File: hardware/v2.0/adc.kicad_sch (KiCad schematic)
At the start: 19 parts, among them IC2 LTC2256CUJ-12#PBF, J7 RSP-122811-01, U1 ECP5U-25F-CABGA256, U11 LT1993CUD-2_PBF, Y2 SG-8018CG 50.000000MHz

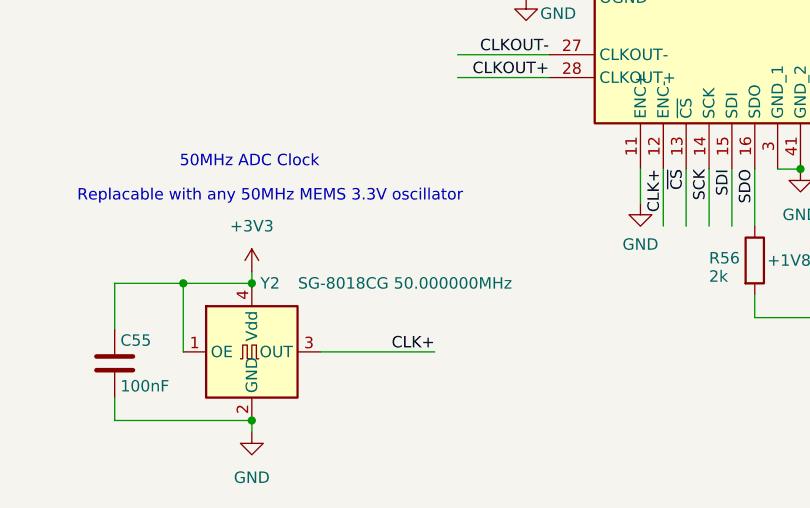
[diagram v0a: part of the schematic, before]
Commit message: HPD line protection
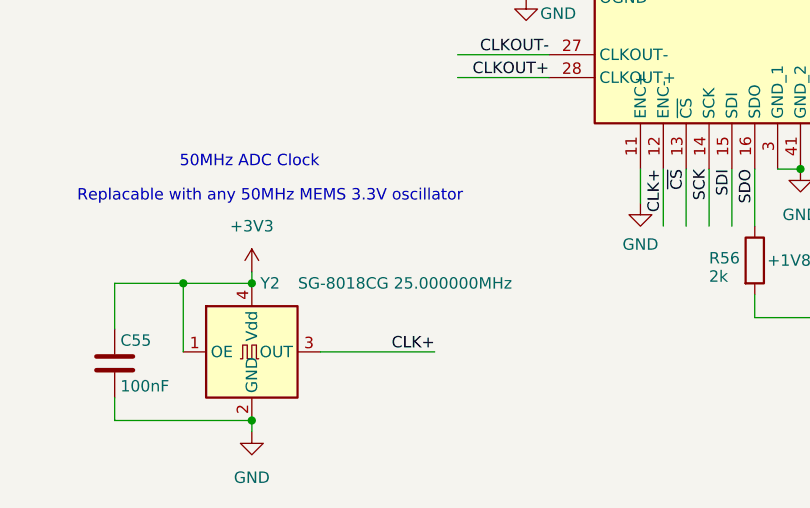
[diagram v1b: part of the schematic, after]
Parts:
- Y2: value SG-8018CG 50.000000MHz -> SG-8018CG 25.000000MHz; LCSC Link https://lcsc.com/product-detail/Programmable-Oscillators_EP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 -> https://www.lcsc.com/product-detail/C21113871.html; LCSC Part # C390526 -> C21113871; Manufactuer Part Number SG-8018CG 50.000000MHz TJHSA -> SG-8018CG 25.0000M-TJHPA3
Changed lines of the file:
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@@
 			)
 		)
-		(property "Value" "SG-8018CG 50.000000MHz"
+		(property "Value" "SG-8018CG 25.000000MHz"
 			(at 110.998 148.59 0)
 			(effects
@@
 			)
 		)
-		(property "LCSC Part #" "C390526"
+		(property "LCSC Part #" "C21113871"
 			(at 93.98 156.21 0)
 			(effects
@@
 			)
 		)
-		(property "LCSC Link" "https://lcsc.com/product-detail/Programmable-Oscillators_EPSON-SG-8018CG-50-000000MHz-TJHSA_C390526.html"
+		(property "LCSC Link" "https://www.lcsc.com/product-detail/C21113871.html"
 			(at 93.98 156.21 0)
 			(effects
@@
 			)
 		)
-		(property "Manufactuer Part Number" "SG-8018CG 50.000000MHz TJHSA"
+		(property "Manufactuer Part Number" "SG-8018CG 25.0000M-TJHPA3"
 			(at 93.98 156.21 0)
 			(effects

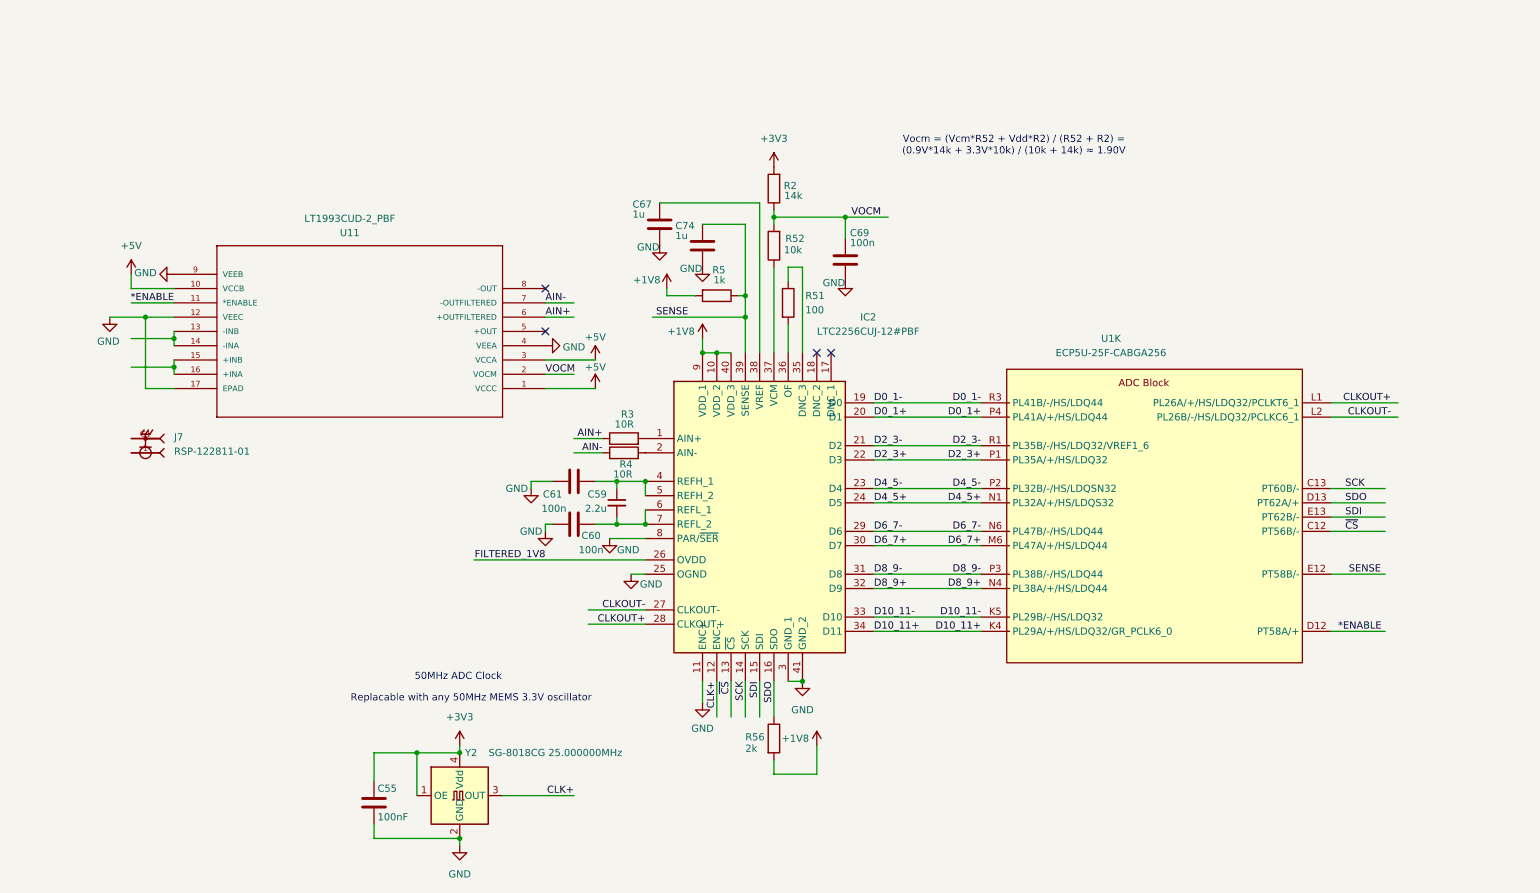
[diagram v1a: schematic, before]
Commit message: ADC driver power and signal input
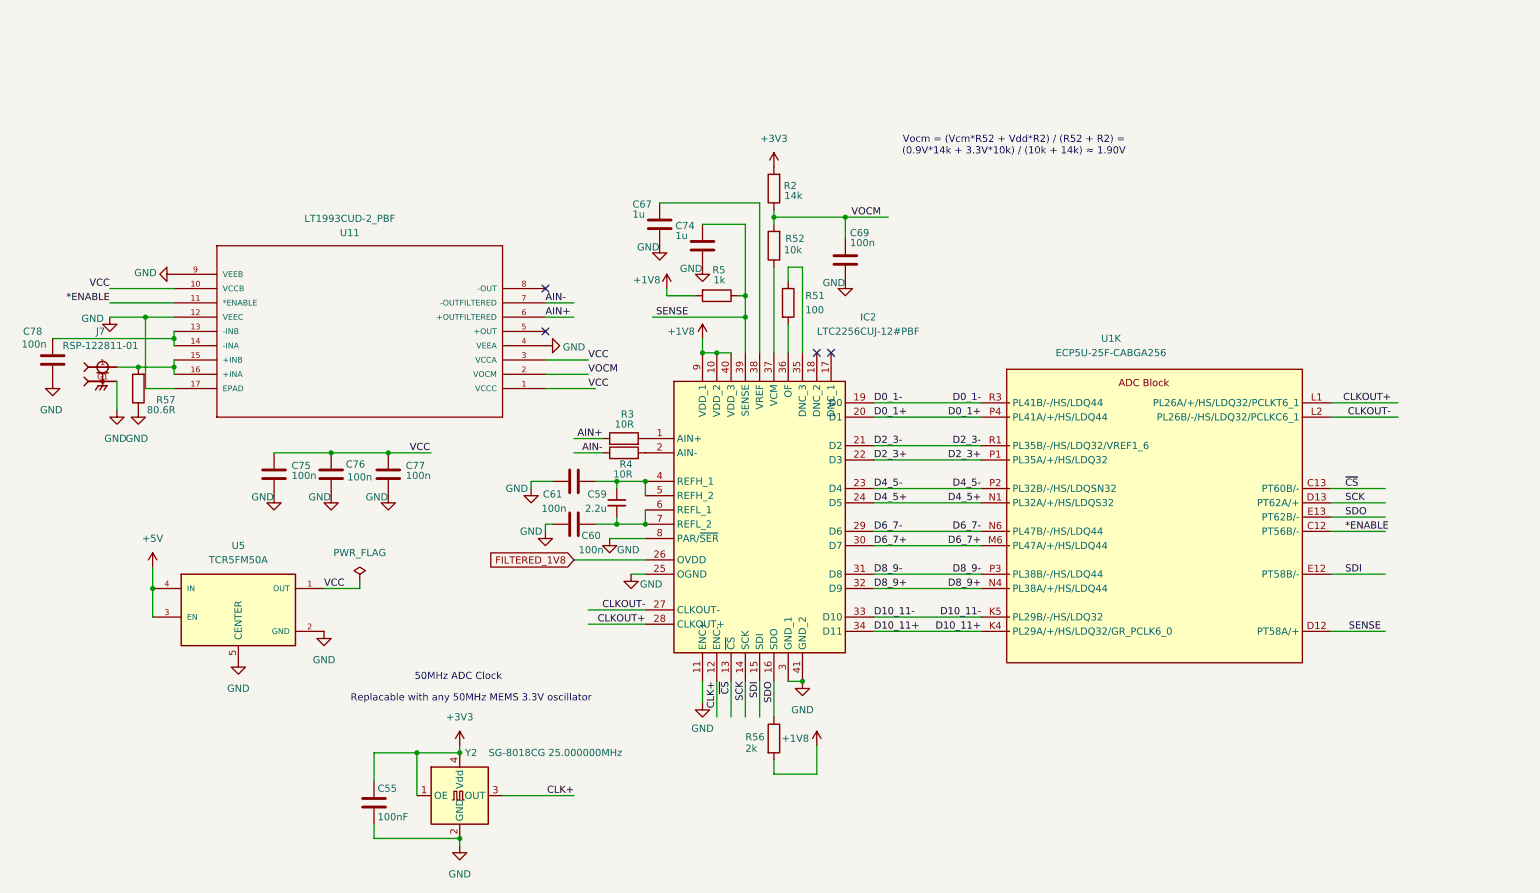
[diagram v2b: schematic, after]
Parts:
- added C75, C76, C77, C78: 100n, Capacitor_SMD:C_0402_1005Metric, symbol Device:C
- added R57: 80.6R, Resistor_SMD:R_0402_1005Metric, symbol Device:R
- added U5: TCR5FM50A, TCR5FM50A:TCR5FM50A, symbol TCR5FM50A:TCR5FM50A
- R3: LCSC Link https://www.lcsc.com/product-detail/C17326083.htm -> https://www.lcsc.com/product-detail/C17693045.html; LCSC Part # C17326083 -> C17693045; Manufactuer Part Number RCS1005F100CS -> RC1005F100CS
- R4: LCSC Link https://www.lcsc.com/product-detail/C17326083.html -> https://www.lcsc.com/product-detail/C17693045.html; LCSC Part # C17326083 -> C17693045; Manufactuer Part Number RCS1005F100CS -> RC1005F100CS
- U11: footprint LT1993CUD-2_PBF:QFN-16_UD -> LT1993CUD_2_PBF:QFN-16_UD
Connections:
- net *ENABLE: now also U1.C12 (PT56B/-); no longer U1.D12 (PT58A/+)
- net +5V: now also U5.3 (EN), U5.4 (IN); no longer U11.1 (VCCC), U11.10 (VCCB), U11.3 (VCCA)
- net GND: now also J7.G1, J7.G2, C75.2, C76.2, C77.2, C78.1, R57.1, U5.2 (GND), U5.5 (CENTER)
- net SCK: now also U1.D13 (PT62A/+); no longer U1.C13 (PT60B/-)
- net SDI: now also U1.E12 (PT58B/-); no longer U1.E13 (PT62B/-)
- net SDO: now also U1.E13 (PT62B/-); no longer U1.D13 (PT62A/+)
- net SENSE: now also U1.D12 (PT58A/+); no longer U1.E12 (PT58B/-)
- net ~{CS}: now also U1.C13 (PT60B/-); no longer U1.C12 (PT56B/-)
- net at U11.13 (-INB), U11.14 (-INA): now also C78.2
- net at U11.15 (+INB), U11.16 (+INA): now also J7.1, R57.2
- new net VCC: C75.1, C76.1, C77.1, U11.1 (VCCC), U11.10 (VCCB), U11.3 (VCCA), U5.1 (OUT)
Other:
- moved on the sheet: J7

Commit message: BOM fields unification for PCBWay requirements
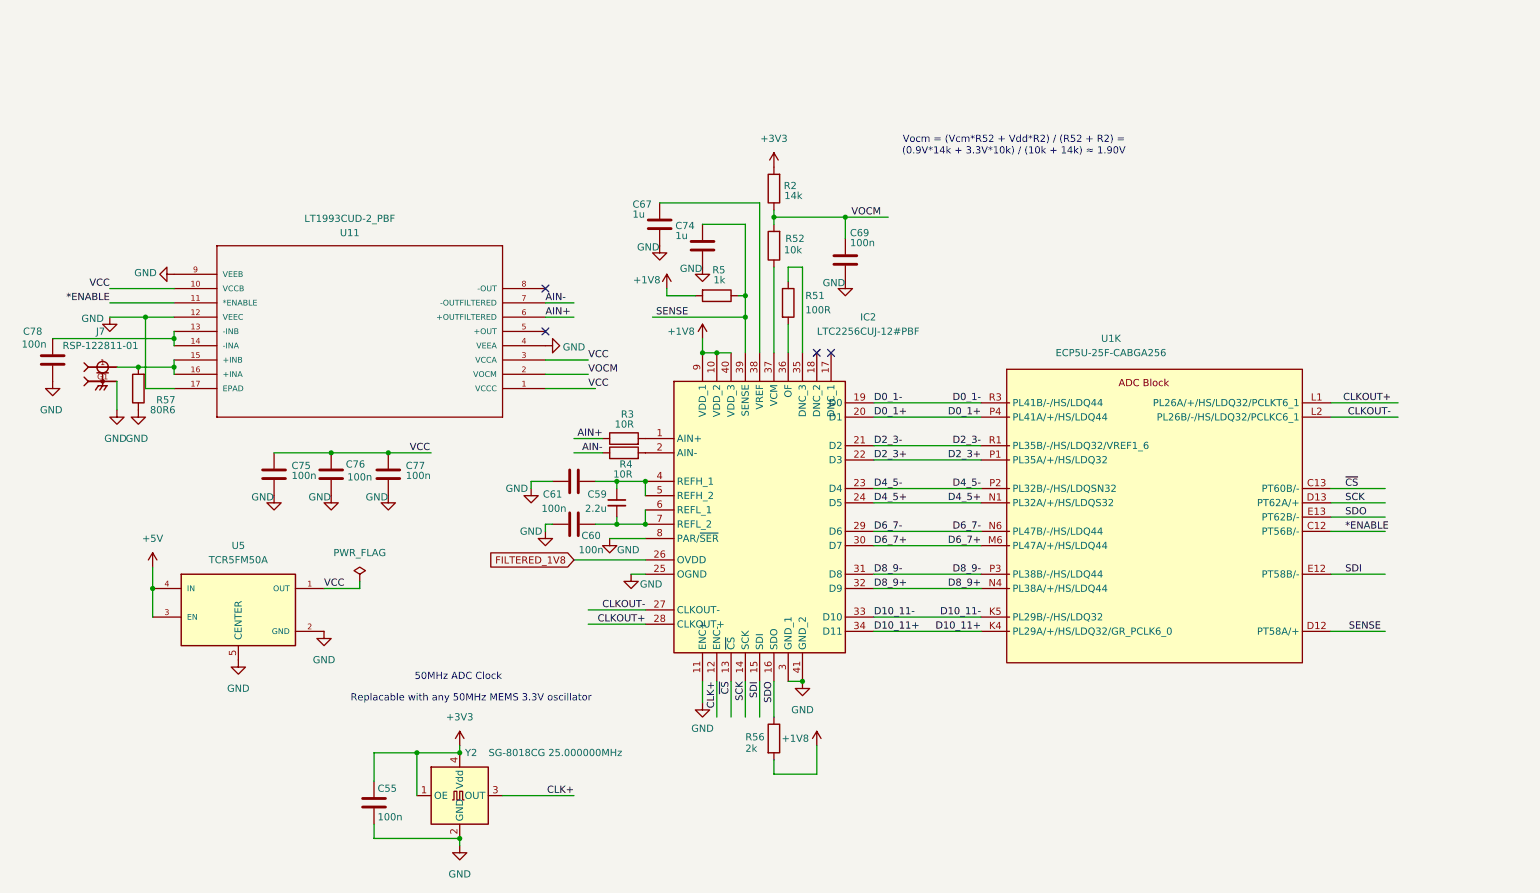
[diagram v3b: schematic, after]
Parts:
- C55: value 100nF -> 100n; MANUFACTURER (none) -> Samsung Electro-Mechanics; MANUFACTURER_PART_NUMBER (none) -> CL05B104KB54PNC
- C59: MANUFACTURER (none) -> Samsung Electro-Mechanics; MANUFACTURER_PART_NUMBER (none) -> CL10A225KP8NNNC
- C60, C61, C69, C75, C76, C77, C78: MANUFACTURER (none) -> Samsung Electro-Mechanics; MANUFACTURER_PART_NUMBER (none) -> CL05B104KB54PNC
- C67, C74: MANUFACTURER (none) -> YAGEO; MANUFACTURER_PART_NUMBER (none) -> CC0402KRX5R6BB105
- IC2: MANUFACTURER (none) -> ADI; MANUFACTURER_PART_NUMBER (none) -> LTC2256CUJ-12#PBF
- J7: MANUFACTURER_PART_NUMBER (none) -> RSP-122811-01
- R2: MANUFACTURER (none) -> UNI-ROYAL; MANUFACTURER_PART_NUMBER (none) -> 0402WGF1402TCE
- R3, R4: MANUFACTURER (none) -> Samsung Electro-Mechanics; MANUFACTURER_PART_NUMBER (none) -> RC1005F100CS
- R5: MANUFACTURER (none) -> UNI-ROYAL; MANUFACTURER_PART_NUMBER (none) -> 0402WGF1001TCE
- R51: value 100 -> 100R; MANUFACTURER (none) -> UNI-ROYAL; MANUFACTURER_PART_NUMBER (none) -> 0402WGF1000TCE
- R52: MANUFACTURER (none) -> UNI-ROYAL; MANUFACTURER_PART_NUMBER (none) -> 0402WGF1002TCE
- R56: MANUFACTURER (none) -> UNI-ROYAL; MANUFACTURER_PART_NUMBER (none) -> 0402WGF2001TCE
- R57: value 80.6R -> 80R6; MANUFACTURER (none) -> Samsung Electro-Mechanics; MANUFACTURER_PART_NUMBER (none) -> RCS1005F80R6CS
- U1: MANUFACTURER (none) -> Lattice; MANUFACTURER_PART_NUMBER (none) -> LFE5U-25F-6BG256C
- U11: MANUFACTURER (none) -> ADI; MANUFACTURER_PART_NUMBER lt1993cud2 -> LT1993CUD-2#PBF
- U5: MANUFACTURER_PART_NUMBER (none) -> TCR5FM50A,RF
- Y2: MANUFACTURER (none) -> EPSON; MANUFACTURER_PART_NUMBER (none) -> SG-8018CG 25.0000M-TJHPA3

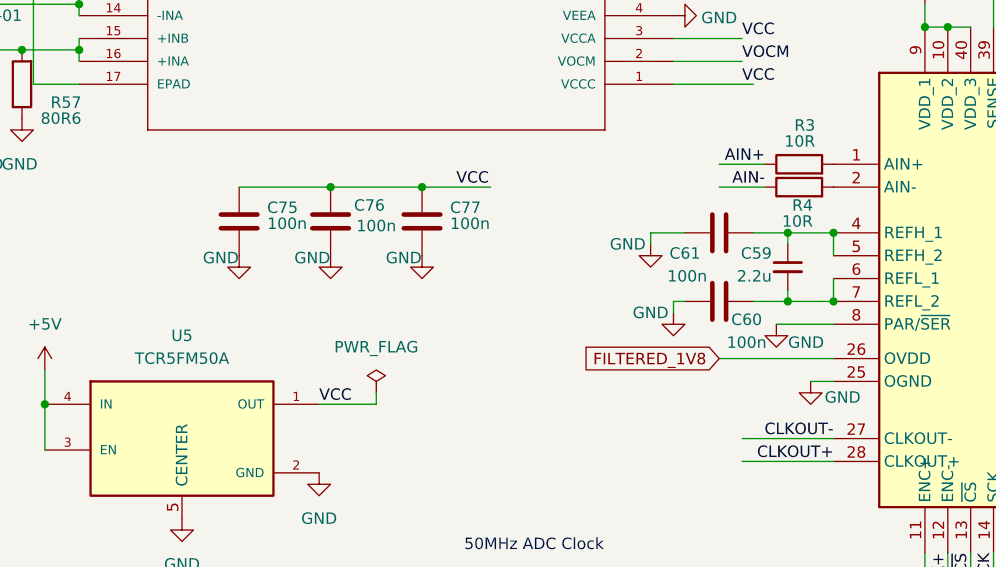
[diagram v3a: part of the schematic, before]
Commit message: ADC datasheet compliance
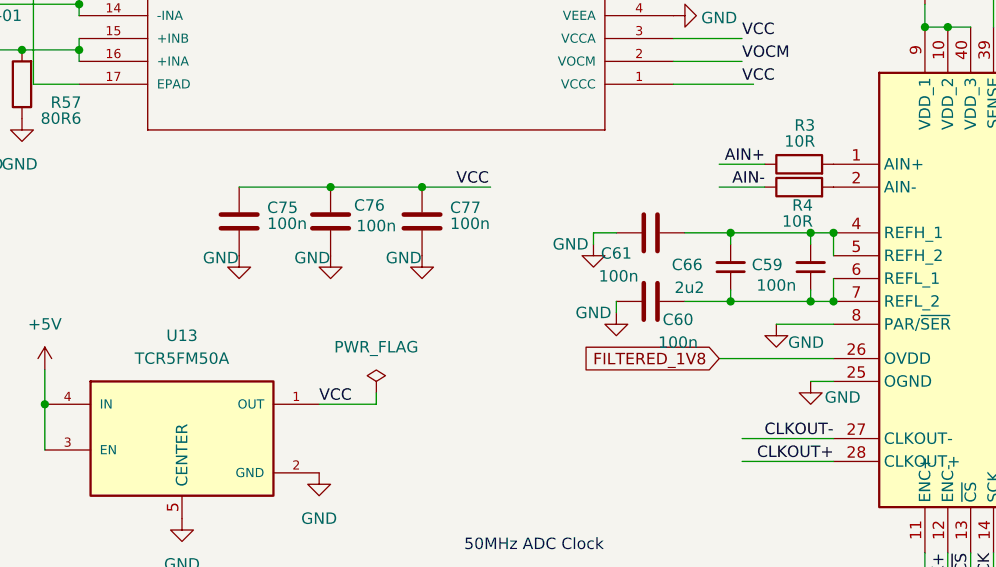
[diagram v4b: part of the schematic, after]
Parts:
- removed U5: TCR5FM50A, TCR5FM50A:TCR5FM50A, symbol TCR5FM50A:TCR5FM50A
- added C66: 2u2, Capacitor_SMD:C_0603_1608Metric, symbol Device:C_Small
- added U13: TCR5FM50A, TCR5FM50A:TCR5FM50A, symbol TCR5FM50A:TCR5FM50A
- C59: value 2.2u -> 100n; footprint Capacitor_SMD:C_0603_1608Metric -> Capacitor_SMD:C_0402_1005Metric; LCSC Link https://www.lcsc.com/product-detail/C1607.html -> https://lcsc.com/product-detail/Multilayer-Ceramic-Capacito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; LCSC Part # C1607 -> C307331; MANUFACTURER_PART_NUMBER CL10A225KP8NNNC -> CL05B104KB54PNC; Manufactuer Part Number CL10A225KP8NNNC -> CL05B104KB54PNC
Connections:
- net +5V: now also U13.3 (EN), U13.4 (IN)
- net GND: now also U13.2 (GND), U13.5 (CENTER)
- net VCC: now also U13.1 (OUT)
- net at C61.2, IC2.4 (REFH_1), IC2.5 (REFH_2): now also C59.2, C66.2; no longer C59.1
- net at C60.2, IC2.6 (REFL_1), IC2.7 (REFL_2): now also C59.1, C66.1; no longer C59.2
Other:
- moved on the sheet: C60, C61
